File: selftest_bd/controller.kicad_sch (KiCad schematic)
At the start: 45 parts, among them U1 Pico

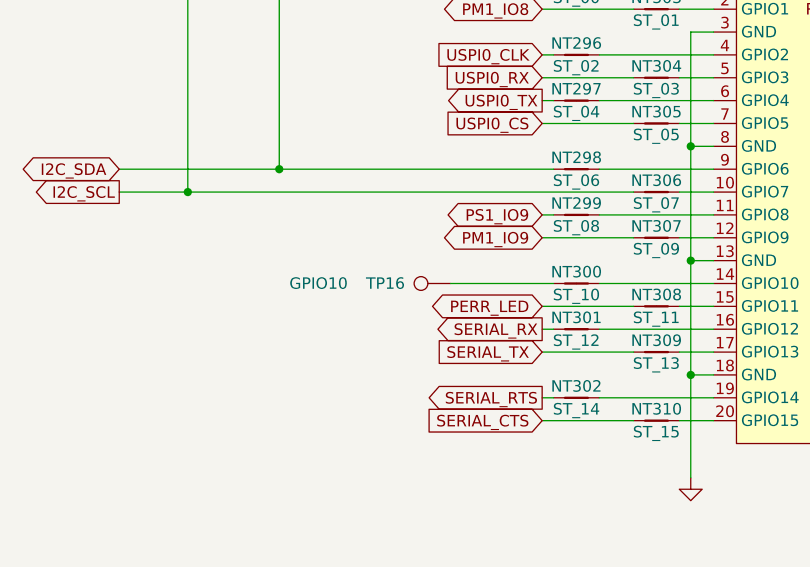
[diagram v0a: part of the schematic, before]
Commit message: Commit V2.0
Redo PCB due to incorrect position of J1 and J2
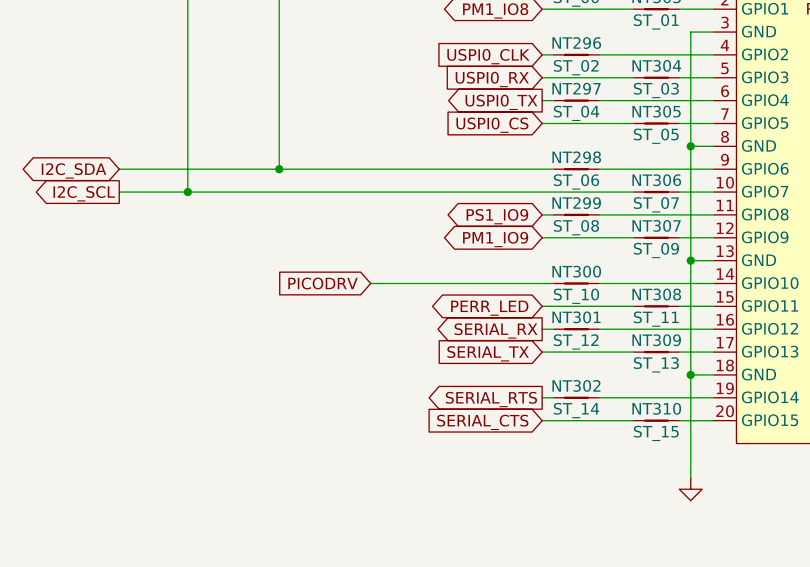
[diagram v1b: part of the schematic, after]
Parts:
- removed TP16: GPIO10, TestPoint:TestPoint_THTPad_D1.5mm_Drill0.7mm, symbol Library:TestPoint
- C2: footprint Capacitor_THT:CP_Radial_D4.0mm_P1.50mm -> Capacitor_THT:CP_Radial_Tantal_D4.5mm_P2.50mm
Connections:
- net PICODRV: now reaches NT300.1
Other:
- title: FIRST TEST STATION SELFTEST BOARD 640-1010-010 -> FIRST TEST STATION SELFTEST BOARD 640-1010-020
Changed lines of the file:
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@@
   (paper "A")
   (title_block
-    (title "FIRST TEST STATION SELFTEST BOARD 640-1010-010")
-    (date "2023-05-16")
-    (rev "1.0")
+    (title "FIRST TEST STATION SELFTEST BOARD 640-1010-020")
+    (date "2023-10-01")
+    (rev "2.0")
   )
   (junction (at 180.34 43.18) (diameter 0) (color 0 0 0 0)
@@
     (stroke (width 0) (type default))
   )
-  (wire (pts (xy 69.85 91.44) (xy 81.28 91.44))
+  (wire (pts (xy 60.96 91.44) (xy 81.28 91.44))
     (stroke (width 0) (type default))
   )
@@
     )
   )
+  (global_label "PICODRV" (shape input) (at 60.96 91.44 180) (fields_autoplaced)
+    (effects (font (size 1.27 1.27)) (justify right))
+    (property "Intersheetrefs" "${INTERSHEET_REFS}" (at 49.9503 91.44 0)
+      (effects (font (size 1.27 1.27)) (justify right) hide)
+    )
+  )
   (global_label "PM1_IO9" (shape bidirectional) (at 80.01 86.36 180) (fields_autoplaced)
     (effects (font (size 1.27 1.27)) (justify right))
@@
     )
   )
-  (symbol (lib_id "Library:TestPoint") (at 69.85 91.44 90) (mirror x) (unit 1)
-    (in_bom yes) (on_board yes) (dnp no)
-    (property "Reference" "TP16" (at 64.77 91.44 90)
-      (effects (font (size 1.27 1.27)) (justify left))
-    )
-    (property "Value" "GPIO10" (at 58.42 91.44 90)
-      (effects (font (size 1.27 1.27)) (justify left))
-    )
-    (property "Footprint" "TestPoint:TestPoint_THTPad_D1.5mm_Drill0.7mm" (at 69.85 96.52 0)
-      (effects (font (size 1.27 1.27)) hide)
-    )
-    (property "Datasheet" "~" (at 69.85 96.52 0)
-      (effects (font (size 1.27 1.27)) hide)
-    )
-    (pin "1")
-    (instances
-      (project "selftest_bd"
-        (path "/e63e39d7-6ac0-4ffd-8aa3-1841a4541b55/0d52fbf2-1bfa-42d9-ae91-95d10277d4e9"
-          (reference "TP16") (unit 1)
-        )
-      )
-    )
-  )
   (symbol (lib_id "Library:NetTie_2") (at 149.86 104.14 0) (mirror y) (unit 1)
     (in_bom yes) (on_board yes) (dnp no)
@@
       (effects (font (size 1.27 1.27)) (justify left))
     )
-    (property "Footprint" "Capacitor_THT:CP_Radial_D4.0mm_P1.50mm" (at 181.3052 39.37 0)
-      (effects (font (size 1.27 1.27)) hide)
-    )
+    (property "Footprint" "Capacitor_THT:CP_Radial_Tantal_D4.5mm_P2.50mm" (at 181.3052 39.37 0)
+      (effects (font (size 1.27 1.27)) hide)
+    )

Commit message: update README and small correction
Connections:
- net PM1_IO8 renamed PM1_IO0
- net PM1_IO9 renamed PM1_IO1
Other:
- title: FIRST TEST STATION SELFTEST BOARD 640-1010-020 -> FIRST TEST STATION SELFTEST BOARD 640-1010-021
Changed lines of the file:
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@@
   (paper "A")
   (title_block
-    (title "FIRST TEST STATION SELFTEST BOARD 640-1010-020")
+    (title "FIRST TEST STATION SELFTEST BOARD 640-1010-021")
     (date "2023-10-01")
-    (rev "2.0")
+    (rev "2.1")
   )
   (junction (at 180.34 43.18) (diameter 0) (color 0 0 0 0)
@@
     )
   )
-  (global_label "PM1_IO8" (shape bidirectional) (at 80.01 60.96 180) (fields_autoplaced)
+  (global_label "PM1_IO0" (shape bidirectional) (at 80.01 60.96 180) (fields_autoplaced)
     (effects (font (size 1.27 1.27)) (justify right))
-    (property "Intersheetrefs" "${INTERSHEET_REFS}" (at 69.5536 60.8806 0)
+    (property "Intersheetrefs" "${INTERSHEET_REFS}" (at 67.9496 60.96 0)
       (effects (font (size 1.27 1.27)) (justify right) hide)
     )
@@
     )
   )
-  (global_label "PM1_IO9" (shape bidirectional) (at 80.01 86.36 180) (fields_autoplaced)
+  (global_label "PM1_IO1" (shape bidirectional) (at 80.01 86.36 180) (fields_autoplaced)
     (effects (font (size 1.27 1.27)) (justify right))
-    (property "Intersheetrefs" "${INTERSHEET_REFS}" (at 69.5536 86.2806 0)
+    (property "Intersheetrefs" "${INTERSHEET_REFS}" (at 67.9496 86.36 0)
       (effects (font (size 1.27 1.27)) (justify right) hide)
     )
